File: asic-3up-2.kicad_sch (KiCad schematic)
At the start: 79 parts, among them J16 Conn_01x01, J17 Conn_01x01, J8 Conn_01x01, J9 Conn_01x01, U57 MCP1824T-1202E/OT, U58 MCP1824T-1202E/OT, U59 MCP1824T-1202E/OT, U60 MCP1824T-0802E, U61 MCP1824T-0802E, U62 MCP1824T-0802E, U63 BM1362AC_MODE1, U64 BM1362AC_MODE0, U65 BM1362AC_MODE1

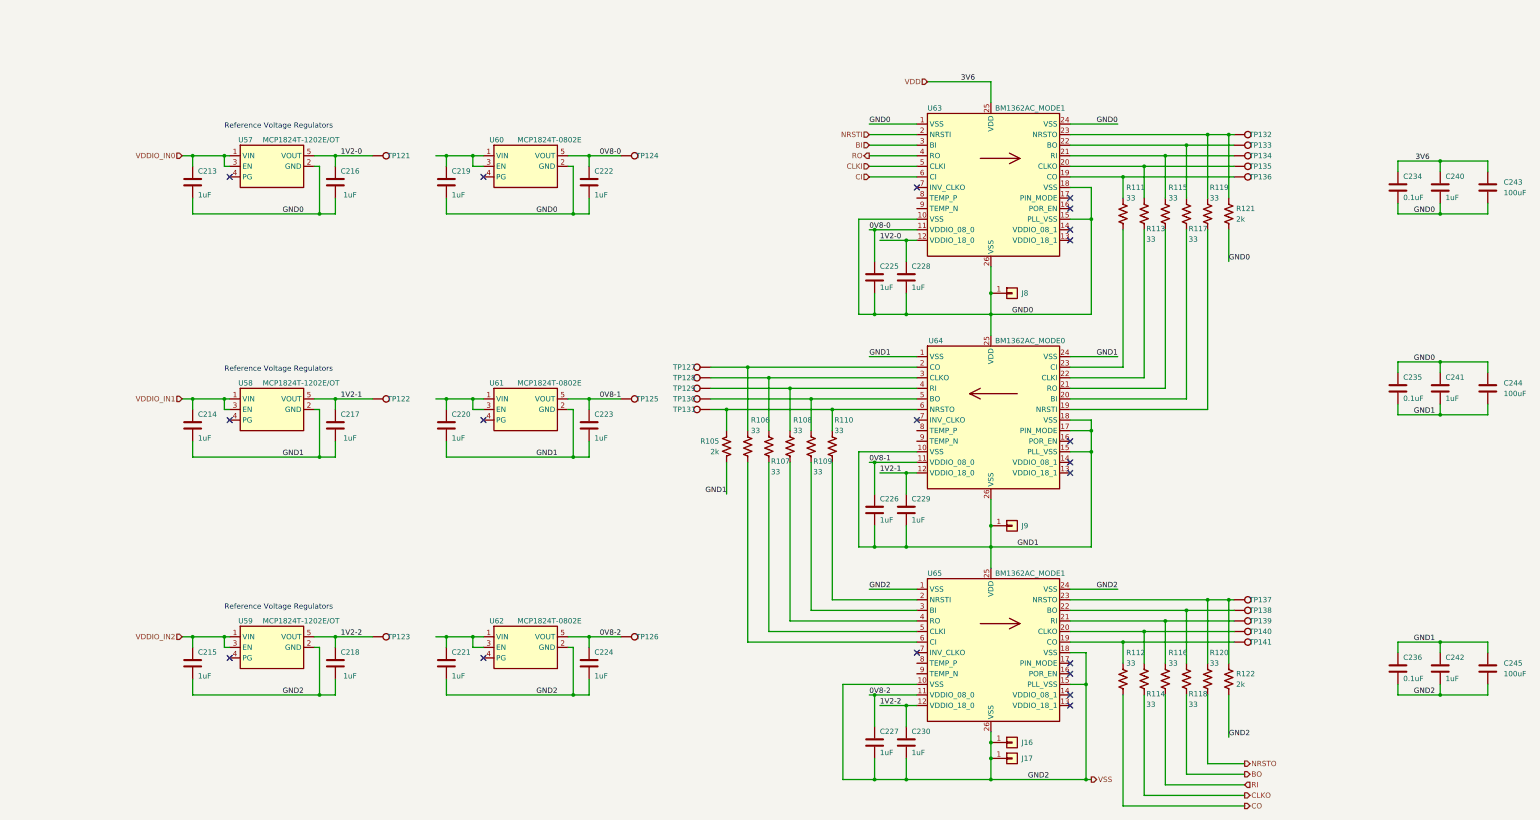
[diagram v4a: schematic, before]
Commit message: forgot that data needs to start with the ASIC that has GND at system GND... reversed everything
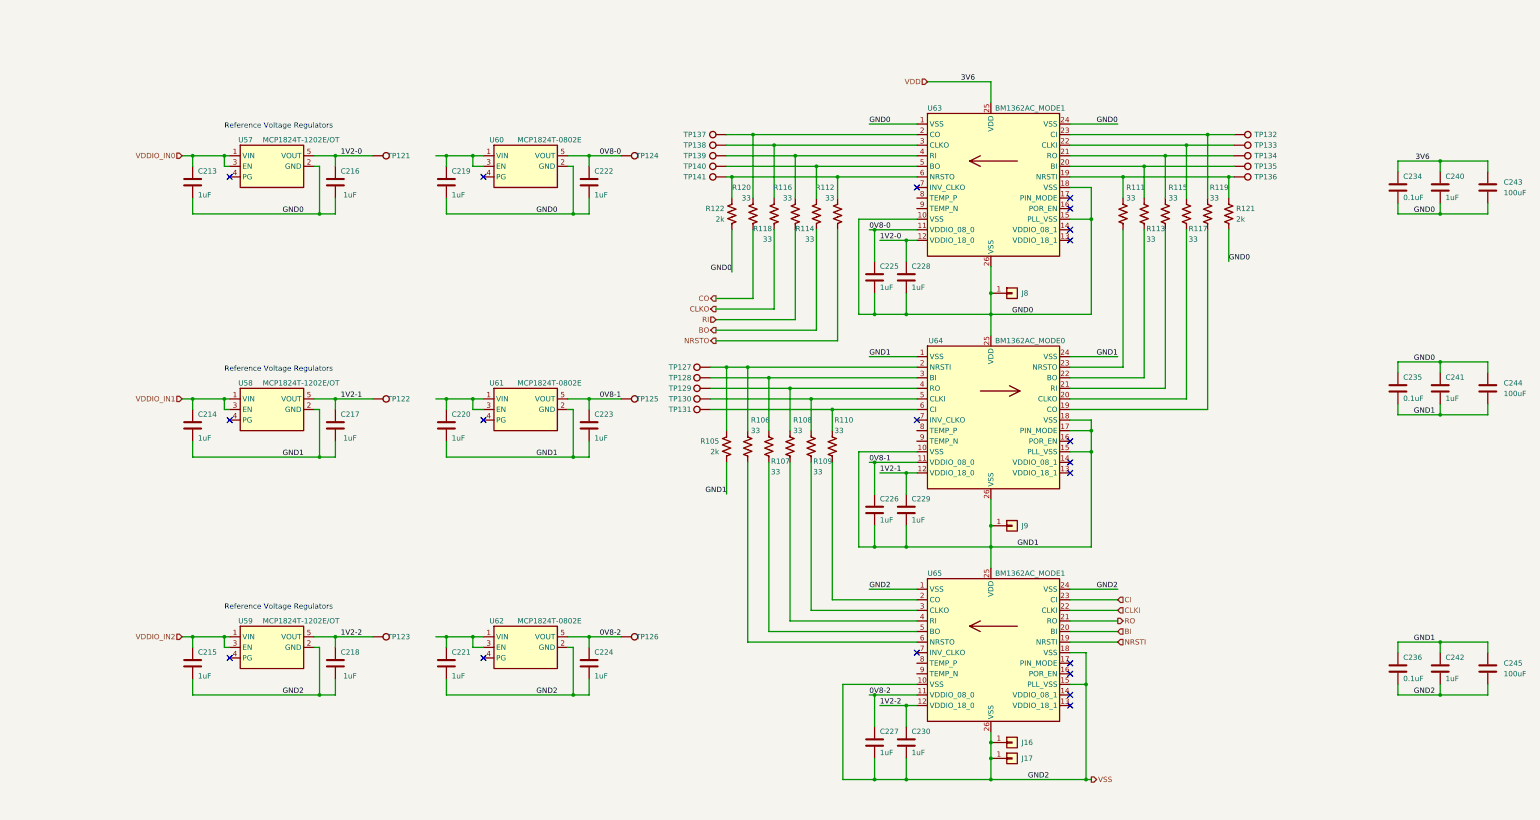
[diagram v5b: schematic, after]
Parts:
- U63, U65: symbol emberone:BM1362AC_MODE1 -> emberone:BM1362AC_MODE0
- U64: symbol emberone:BM1362AC_MODE0 -> emberone:BM1362AC_MODE1
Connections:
- net BI: now also U65.20 (BI); no longer U63.3 (BI)
- net BO: now also R114.2; no longer R118.2
- net CI: now also U65.23 (CI); no longer U63.6 (CI)
- net CLKI: now also U65.22 (CLKI); no longer U63.5 (CLKI)
- net CLKO: now also R118.2; no longer R114.2
- net CO: now also R120.2; no longer R112.2
- net GND0: now also R122.2
- net NRSTI: now also U65.19 (NRSTI); no longer U63.2 (NRSTI)
- net NRSTO: now also R112.2; no longer R120.2
- net RO: now also U65.21 (RO); no longer U63.4 (RO)
- net VSS: no longer R122.2
- net at R119.1, TP132.1, U63.23 (CI): no longer R121.1
- net at R106.1, TP127.1, U64.2 (NRSTI): now also R105.1
- net at R111.1, TP136.1, U63.19 (NRSTI): now also R121.1
- net at R120.1, TP137.1: now also U63.2 (CO); no longer R122.1, U65.23 (NRSTO)
- net at R110.1, TP131.1, U64.6 (CI): no longer R105.1
- net at R114.1, TP140.1: now also U63.5 (BO); no longer U65.20 (CLKO)
- net at R112.1, TP141.1: now also R122.1, U63.6 (NRSTO); no longer U65.19 (CO)
- net at R116.1, TP139.1: now also U63.4 (RI); no longer U65.21 (RI)
- net at R118.1, TP138.1: now also U63.3 (CLKO); no longer U65.22 (BO)
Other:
- moved on the sheet: R112, R114, R116, R118, R120, R122, TP137, TP138, TP139, TP140, TP141

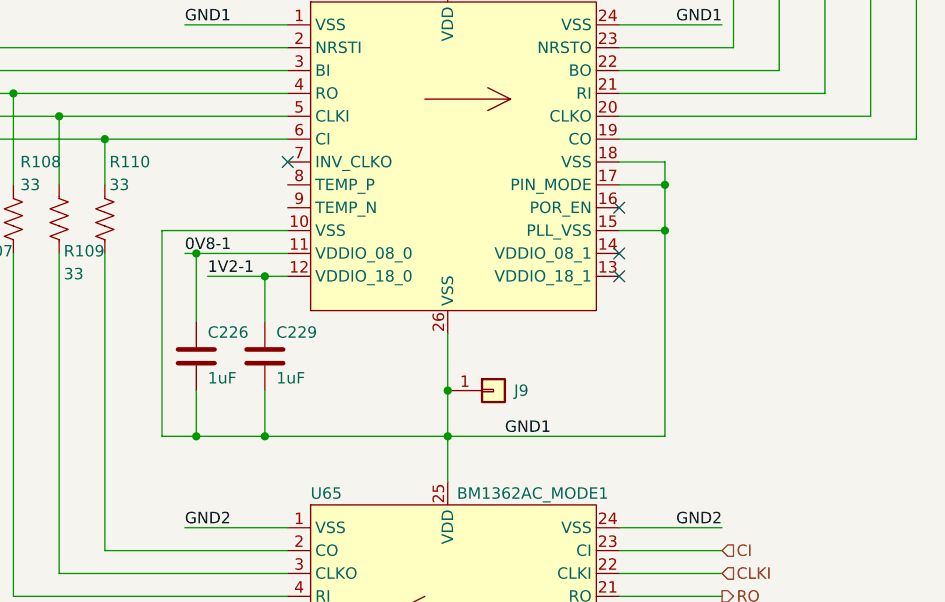
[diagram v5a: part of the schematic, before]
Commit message: added the heatsink mounting holes
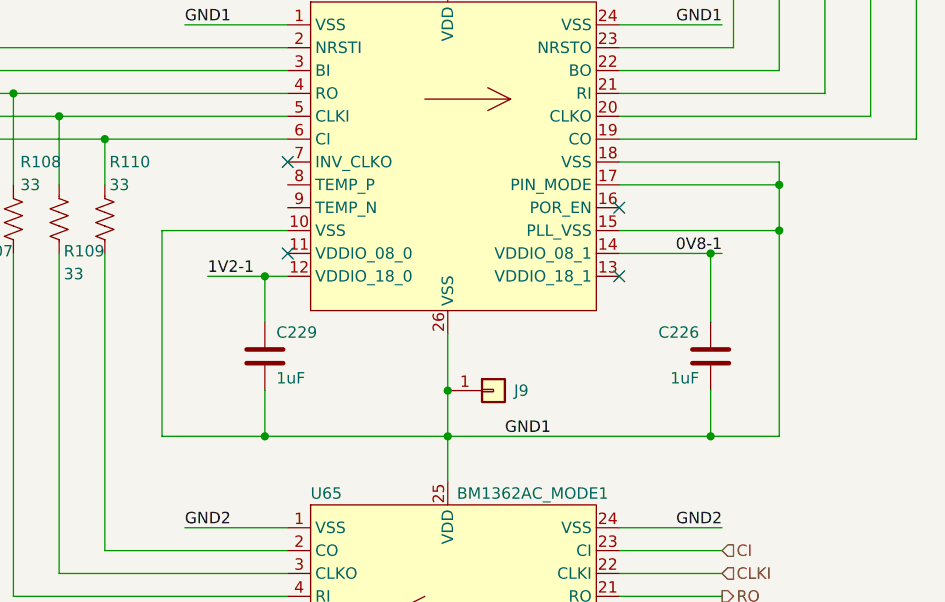
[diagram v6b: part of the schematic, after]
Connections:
- net 0V8-1: now also U64.14 (VDDIO_08_1); no longer U64.11 (VDDIO_08_0)
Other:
- moved on the sheet: C226
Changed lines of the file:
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@@
 	)
 	(junction
-		(at 228.6 85.09)
+		(at 278.13 138.43)
 		(diameter 0)
 		(color 0 0 0 0)
 	)
 	(junction
-		(at 273.05 130.81)
+		(at 228.6 85.09)
 		(diameter 0)
 		(color 0 0 0 0)
@@
 	)
 	(junction
-		(at 273.05 135.89)
-		(diameter 0)
-		(color 0 0 0 0)
-	)
-	(junction
 		(at 300.99 59.69)
 		(diameter 0)
@@
 	)
 	(junction
-		(at 220.98 158.75)
-		(diameter 0)
-		(color 0 0 0 0)
-	)
-	(junction
 		(at 124.46 123.19)
 		(diameter 0)
@@
 	)
 	(junction
+		(at 278.13 158.75)
+		(diameter 0)
+		(color 0 0 0 0)
+	)
+	(junction
 		(at 186.69 69.85)
 		(diameter 0)
@@
 	)
 	(junction
-		(at 220.98 138.43)
-		(diameter 0)
-		(color 0 0 0 0)
-	)
-	(junction
 		(at 124.46 180.34)
 		(diameter 0)
@@
 	)
 	(junction
+		(at 285.75 130.81)
+		(diameter 0)
+		(color 0 0 0 0)
+	)
+	(junction
 		(at 248.92 153.67)
 		(diameter 0)
@@
 	)
 	(junction
+		(at 285.75 135.89)
+		(diameter 0)
+		(color 0 0 0 0)
+	)
+	(junction
 		(at 210.82 125.73)
 		(diameter 0)
@@
 	)
 	(no_connect
+		(at 231.14 138.43)
+	)
+	(no_connect
 		(at 267.97 133.35)
 	)
@@
 		(at 231.14 72.39)
 	)
-	(no_connect
-		(at 267.97 138.43)
-	)
 	(wire
 		(pts
@@
 	(wire
 		(pts
-			(xy 273.05 130.81) (xy 273.05 128.27)
+			(xy 285.75 130.81) (xy 285.75 128.27)
 		)
 		(stroke
@@
 	(wire
 		(pts
-			(xy 273.05 135.89) (xy 273.05 130.81)
+			(xy 278.13 158.75) (xy 285.75 158.75)
+		)
+		(stroke
+			(width 0)
+			(type default)
+		)
+	)
+	(wire
+		(pts
+			(xy 285.75 135.89) (xy 285.75 130.81)
 		)
 		(stroke
@@
 	(wire
 		(pts
-			(xy 220.98 138.43) (xy 231.14 138.43)
+			(xy 278.13 138.43) (xy 267.97 138.43)
 		)
 		(stroke
@@
 	(wire
 		(pts
-			(xy 220.98 138.43) (xy 220.98 146.05)
+			(xy 278.13 138.43) (xy 278.13 146.05)
 		)
 		(stroke
@@
 	(wire
 		(pts
-			(xy 267.97 130.81) (xy 273.05 130.81)
+			(xy 267.97 130.81) (xy 285.75 130.81)
 		)
 		(stroke
@@
 	(wire
 		(pts
-			(xy 267.97 135.89) (xy 273.05 135.89)
+			(xy 267.97 135.89) (xy 285.75 135.89)
 		)
 		(stroke
@@
 	(wire
 		(pts
-			(xy 273.05 128.27) (xy 267.97 128.27)
+			(xy 285.75 128.27) (xy 267.97 128.27)
 		)
 		(stroke
@@
 	(wire
 		(pts
-			(xy 220.98 153.67) (xy 220.98 158.75)
+			(xy 278.13 153.67) (xy 278.13 158.75)
 		)
 		(stroke
@@
 	(wire
 		(pts
-			(xy 248.92 158.75) (xy 273.05 158.75)
+			(xy 248.92 158.75) (xy 278.13 158.75)
 		)
 		(stroke
@@
 	(wire
 		(pts
-			(xy 217.17 158.75) (xy 220.98 158.75)
+			(xy 217.17 158.75) (xy 228.6 158.75)
 		)
 		(stroke
@@
 	(wire
 		(pts
-			(xy 273.05 158.75) (xy 273.05 135.89)
+			(xy 285.75 158.75) (xy 285.75 135.89)
 		)
 		(stroke
@@
 	(wire
 		(pts
-			(xy 220.98 158.75) (xy 228.6 158.75)
-		)
-		(stroke
-			(width 0)
-			(type default)
-		)
-	)
-	(wire
-		(pts
 			(xy 118.11 64.77) (xy 118.11 67.31)
 		)
@@
 	(wire
 		(pts
-			(xy 219.71 138.43) (xy 220.98 138.43)
+			(xy 278.13 138.43) (xy 279.4 138.43)
 		)
 		(stroke
@@
 	)
 	(label "0V8-1"
-		(at 219.71 138.43 0)
+		(at 279.4 138.43 180)
 		(fields_autoplaced yes)
 		(effects
@@
 				(size 1.27 1.27)
 			)
-			(justify left bottom)
+			(justify right bottom)
 		)
 	)
@@
 	(symbol
 		(lib_id "Device:C")
-		(at 220.98 149.86 0)
+		(at 278.13 149.86 0)
+		(mirror y)
 		(unit 1)
 		(exclude_from_sim no)
@@
 		(dnp no)
 		(property "Reference" "C226"
-			(at 222.25 147.955 0)
+			(at 276.86 147.955 0)
 			(effects
 				(font
@@
 		)
 		(property "Value" "1uF"
-			(at 222.25 153.035 0)
+			(at 276.86 153.035 0)
 			(effects
 				(font
@@
 		)
 		(property "Footprint" "Capacitor_SMD:C_0402_1005Metric"
-			(at 220.98 149.86 0)
+			(at 278.13 149.86 0)
 			(effects
 				(font
@@
 		)
 		(property "Datasheet" ""
-			(at 220.98 149.86 0)
+			(at 278.13 149.86 0)
 			(effects
 				(font
@@
 		)
 		(property "Description" ""
-			(at 220.98 149.86 0)
+			(at 278.13 149.86 0)
 			(effects
 				(font
@@
 		)
 		(property "DK" "587-5514-1-ND"
-			(at 220.98 149.86 0)
+			(at 278.13 149.86 0)
 			(effects
 				(font
@@
 		)
 		(property "PARTNO" "EMK105BJ105MV-F"
-			(at 220.98 149.86 0)
+			(at 278.13 149.86 0)
 			(effects
 				(font

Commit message: placements done. shrunk test points
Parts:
- TP121, TP122, TP123, TP124, TP125, TP126, TP127, TP128, TP129, TP130, TP131, TP132, TP133, TP134, TP135, TP136, TP137, TP138, TP139, TP140, TP141: footprint TestPoint:TestPoint_Pad_D1.5mm -> TestPoint:TestPoint_Pad_D1.0mm
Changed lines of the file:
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@@
 			)
 		)
-		(property "Footprint" "TestPoint:TestPoint_Pad_D1.5mm"
+		(property "Footprint" "TestPoint:TestPoint_Pad_D1.0mm"
 			(at 160.02 175.26 0)
 			(effects
@@
 			)
 		)
-		(property "Footprint" "TestPoint:TestPoint_Pad_D1.5mm"
+		(property "Footprint" "TestPoint:TestPoint_Pad_D1.0mm"
 			(at 160.02 118.11 0)
 			(effects
@@
 			)
 		)
-		(property "Footprint" "TestPoint:TestPoint_Pad_D1.5mm"
+		(property "Footprint" "TestPoint:TestPoint_Pad_D1.0mm"
 			(at 307.34 64.77 0)
 			(effects
@@
 			)
 		)
-		(property "Footprint" "TestPoint:TestPoint_Pad_D1.5mm"
+		(property "Footprint" "TestPoint:TestPoint_Pad_D1.0mm"
 			(at 181.61 120.65 0)
 			(effects
@@
 			)
 		)
-		(property "Footprint" "TestPoint:TestPoint_Pad_D1.5mm"
+		(property "Footprint" "TestPoint:TestPoint_Pad_D1.0mm"
 			(at 307.34 74.93 0)
 			(effects
@@
 			)
 		)
-		(property "Footprint" "TestPoint:TestPoint_Pad_D1.5mm"
+		(property "Footprint" "TestPoint:TestPoint_Pad_D1.0mm"
 			(at 185.42 64.77 0)
 			(effects
@@
 			)
 		)
-		(property "Footprint" "TestPoint:TestPoint_Pad_D1.5mm"
+		(property "Footprint" "TestPoint:TestPoint_Pad_D1.0mm"
 			(at 307.34 67.31 0)
 			(effects
@@
 			)
 		)
-		(property "Footprint" "TestPoint:TestPoint_Pad_D1.5mm"
+		(property "Footprint" "TestPoint:TestPoint_Pad_D1.0mm"
 			(at 307.34 69.85 0)
 			(effects
@@
 			)
 		)
-		(property "Footprint" "TestPoint:TestPoint_Pad_D1.5mm"
+		(property "Footprint" "TestPoint:TestPoint_Pad_D1.0mm"
 			(at 185.42 69.85 0)
 			(effects
@@
 			)
 		)
-		(property "Footprint" "TestPoint:TestPoint_Pad_D1.5mm"
+		(property "Footprint" "TestPoint:TestPoint_Pad_D1.0mm"
 			(at 185.42 72.39 0)
 			(effects
@@
 			)
 		)
-		(property "Footprint" "TestPoint:TestPoint_Pad_D1.5mm"
+		(property "Footprint" "TestPoint:TestPoint_Pad_D1.0mm"
 			(at 100.33 118.11 0)
 			(effects
@@
 			)
 		)
-		(property "Footprint" "TestPoint:TestPoint_Pad_D1.5mm"
+		(property "Footprint" "TestPoint:TestPoint_Pad_D1.0mm"
 			(at 185.42 67.31 0)
 			(effects
@@
 			)
 		)
-		(property "Footprint" "TestPoint:TestPoint_Pad_D1.5mm"
+		(property "Footprint" "TestPoint:TestPoint_Pad_D1.0mm"
 			(at 307.34 72.39 0)
 			(effects
@@
 			)
 		)
-		(property "Footprint" "TestPoint:TestPoint_Pad_D1.5mm"
+		(property "Footprint" "TestPoint:TestPoint_Pad_D1.0mm"
 			(at 100.33 59.69 0)
 			(effects
@@
 			)
 		)
-		(property "Footprint" "TestPoint:TestPoint_Pad_D1.5mm"
+		(property "Footprint" "TestPoint:TestPoint_Pad_D1.0mm"
 			(at 185.42 74.93 0)
 			(effects
@@
 			)
 		)
-		(property "Footprint" "TestPoint:TestPoint_Pad_D1.5mm"
+		(property "Footprint" "TestPoint:TestPoint_Pad_D1.0mm"
 			(at 160.02 59.69 0)
 			(effects
@@
 			)
 		)
-		(property "Footprint" "TestPoint:TestPoint_Pad_D1.5mm"
+		(property "Footprint" "TestPoint:TestPoint_Pad_D1.0mm"
 			(at 100.33 175.26 0)
 			(effects
@@
 			)
 		)
-		(property "Footprint" "TestPoint:TestPoint_Pad_D1.5mm"
+		(property "Footprint" "TestPoint:TestPoint_Pad_D1.0mm"
 			(at 181.61 125.73 0)
 			(effects
@@
 			)
 		)
-		(property "Footprint" "TestPoint:TestPoint_Pad_D1.5mm"
+		(property "Footprint" "TestPoint:TestPoint_Pad_D1.0mm"
 			(at 181.61 123.19 0)
 			(effects
@@
 			)
 		)
-		(property "Footprint" "TestPoint:TestPoint_Pad_D1.5mm"
+		(property "Footprint" "TestPoint:TestPoint_Pad_D1.0mm"
 			(at 181.61 128.27 0)
 			(effects
@@
 			)
 		)
-		(property "Footprint" "TestPoint:TestPoint_Pad_D1.5mm"
+		(property "Footprint" "TestPoint:TestPoint_Pad_D1.0mm"
 			(at 181.61 130.81 0)
 			(effects
